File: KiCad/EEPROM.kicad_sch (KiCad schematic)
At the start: 2 parts, among them U1 24LC256

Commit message: Arreglada la EEPROM
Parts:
- renumbered U1 to U10
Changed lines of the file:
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@@
 		(on_board yes)
 		(dnp no)
-		(property "Reference" "C1"
+		(property "Reference" "C?"
 			(at 128.27 92.456 0)
 			(effects
@@
 				(path "/b59472fa-fde6-436b-a51b-1bcdb1fd69b0"
 					(reference "C1")
+					(unit 1)
+				)
+			)
+			(project "SEIENTS_EDD"
+				(path "/b6401b4f-5426-49b8-bb2e-8ecdb19989ef/e3788a6e-8f47-444e-9f2c-8c4ecda69c18"
+					(reference "C?")
 					(unit 1)
 				)
@@
 		(dnp no)
 		(fields_autoplaced yes)
-		(property "Reference" "#PWR05"
+		(property "Reference" "#PWR036"
 			(at 125.73 115.57 0)
 			(effects
@@
 		(dnp no)
 		(fields_autoplaced yes)
-		(property "Reference" "#PWR06"
+		(property "Reference" "#PWR?"
 			(at 162.56 109.22 0)
 			(effects
@@
 				(path "/b59472fa-fde6-436b-a51b-1bcdb1fd69b0"
 					(reference "#PWR06")
+					(unit 1)
+				)
+			)
+			(project "SEIENTS_EDD"
+				(path "/b6401b4f-5426-49b8-bb2e-8ecdb19989ef/e3788a6e-8f47-444e-9f2c-8c4ecda69c18"
+					(reference "#PWR?")
 					(unit 1)
 				)
@@
 		(dnp no)
 		(fields_autoplaced yes)
-		(property "Reference" "U1"
+		(property "Reference" "U10"
 			(at 150.7333 87.63 0)
 			(effects
@@
 		(dnp no)
 		(fields_autoplaced yes)
-		(property "Reference" "#PWR04"
+		(property "Reference" "#PWR035"
 			(at 148.59 115.57 0)
 			(effects
@@
 		(dnp no)
 		(fields_autoplaced yes)
-		(property "Reference" "#PWR01"
+		(property "Reference" "#PWR?"
 			(at 134.62 115.57 0)
 			(effects
@@
 					(unit 1)
 				)
+			)
+			(project "SEIENTS_EDD"
+				(path "/b6401b4f-5426-49b8-bb2e-8ecdb19989ef/e3788a6e-8f47-444e-9f2c-8c4ecda69c18"
+					(reference "#PWR?")
+					(unit 1)
+				)

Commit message: Arreglat el DE-9
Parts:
- renumbered C1 to C20
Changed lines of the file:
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@@
+	)
+	(junction
+		(at 134.62 109.22)
+		(diameter 0)
+		(color 0 0 0 0)
 	)
 	(junction
@@
 		(on_board yes)
 		(dnp no)
-		(property "Reference" "C?"
-			(at 128.27 92.456 0)
+		(property "Reference" "C20"
+			(at 128.778 94.488 0)
 			(effects
 				(font
@@
 			(project "SEIENTS_EDD"
 				(path "/b6401b4f-5426-49b8-bb2e-8ecdb19989ef/e3788a6e-8f47-444e-9f2c-8c4ecda69c18"
-					(reference "C?")
+					(reference "C20")
 					(unit 1)
 				)
@@
 		(dnp no)
 		(fields_autoplaced yes)
-		(property "Reference" "#PWR?"
+		(property "Reference" "#PWR0101"
 			(at 162.56 109.22 0)
 			(effects
@@
 			(project "SEIENTS_EDD"
 				(path "/b6401b4f-5426-49b8-bb2e-8ecdb19989ef/e3788a6e-8f47-444e-9f2c-8c4ecda69c18"
-					(reference "#PWR?")
+					(reference "#PWR0101")
 					(unit 1)
 				)
@@
 	)
 	(symbol
+		(lib_id "power:PWR_FLAG")
+		(at 134.62 109.22 270)
+		(unit 1)
+		(exclude_from_sim no)
+		(in_bom yes)
+		(on_board yes)
+		(dnp no)
+		(fields_autoplaced yes)
+		(property "Reference" "#FLG05"
+			(at 136.525 109.22 0)
+			(effects
+				(font
+					(size 1.27 1.27)
+				)
+				(hide yes)
+			)
+		)
+		(property "Value" "PWR_FLAG"
+			(at 138.43 109.2199 90)
+			(effects
+				(font
+					(size 1.27 1.27)
+				)
+				(justify left)
+			)
+		)
+		(property "Footprint" ""
+			(at 134.62 109.22 0)
+			(effects
+				(font
+					(size 1.27 1.27)
+				)
+				(hide yes)
+			)
+		)
+		(property "Datasheet" "~"
+			(at 134.62 109.22 0)
+			(effects
+				(font
+					(size 1.27 1.27)
+				)
+				(hide yes)
+			)
+		)
+		(property "Description" "Special symbol for telling ERC where power comes from"
+			(at 134.62 109.22 0)
+			(effects
+				(font
+					(size 1.27 1.27)
+				)
+				(hide yes)
+			)
+		)
+		(pin "1"
+		)
+		(instances
+			(project ""
+				(path "/b6401b4f-5426-49b8-bb2e-8ecdb19989ef/e3788a6e-8f47-444e-9f2c-8c4ecda69c18"
+					(reference "#FLG05")
+					(unit 1)
+				)
+			)
+		)
+	)
+	(symbol
 		(lib_id "power:GND")
 		(at 134.62 109.22 0)
@@
 		(dnp no)
 		(fields_autoplaced yes)
-		(property "Reference" "#PWR?"
+		(property "Reference" "#PWR0102"
 			(at 134.62 115.57 0)
 			(effects
@@
 			(project "SEIENTS_EDD"
 				(path "/b6401b4f-5426-49b8-bb2e-8ecdb19989ef/e3788a6e-8f47-444e-9f2c-8c4ecda69c18"
-					(reference "#PWR?")
-					(unit 1)
-				)
+					(reference "#PWR0102")
+					(unit 1)
+				)

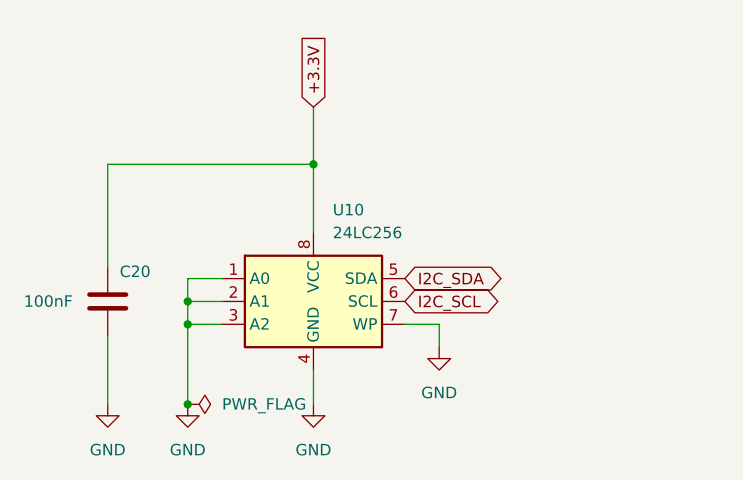
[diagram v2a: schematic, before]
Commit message: ArregLATS ERRORS ERC
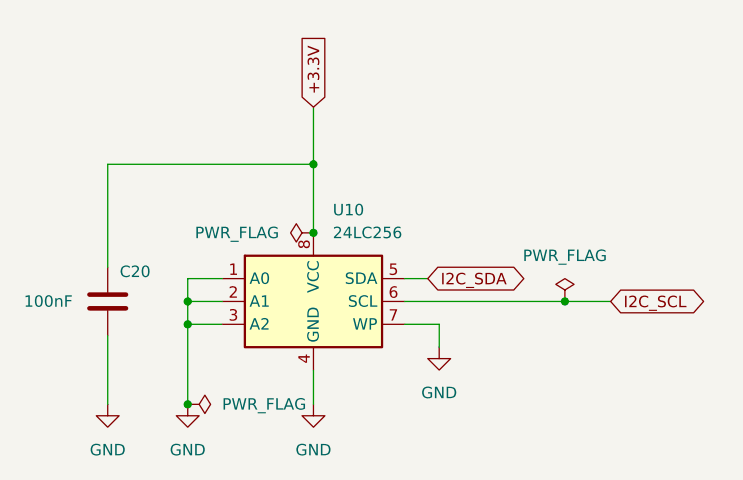
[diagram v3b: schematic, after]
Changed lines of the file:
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@@
+	)
+	(junction
+		(at 176.53 97.79)
+		(diameter 0)
+		(color 0 0 0 0)
+	)
+	(junction
+		(at 148.59 90.17)
+		(diameter 0)
+		(color 0 0 0 0)
 	)
 	(junction
@@
 	(wire
 		(pts
+			(xy 176.53 97.79) (xy 158.75 97.79)
+		)
+		(stroke
+			(width 0)
+			(type default)
+		)
+	)
+	(wire
+		(pts
 			(xy 148.59 105.41) (xy 148.59 109.22)
 		)
@@
 	(wire
 		(pts
+			(xy 161.29 95.25) (xy 158.75 95.25)
+		)
+		(stroke
+			(width 0)
+			(type default)
+		)
+	)
+	(wire
+		(pts
 			(xy 158.75 100.33) (xy 162.56 100.33)
+		)
+		(stroke
+			(width 0)
+			(type default)
+		)
+	)
+	(wire
+		(pts
+			(xy 181.61 97.79) (xy 176.53 97.79)
 		)
 		(stroke
@@
 	(global_label "I2C_SDA"
 		(shape bidirectional)
-		(at 158.75 95.25 0)
+		(at 161.29 95.25 0)
 		(fields_autoplaced yes)
 		(effects
@@
 		)
 		(property "Intersheetrefs" "${INTERSHEET_REFS}"
-			(at 170.4665 95.25 0)
+			(at 173.0065 95.25 0)
 			(effects
 				(font
@@
 	(global_label "I2C_SCL"
 		(shape bidirectional)
-		(at 158.75 97.79 0)
+		(at 181.61 97.79 0)
 		(fields_autoplaced yes)
 		(effects
@@
 		)
 		(property "Intersheetrefs" "${INTERSHEET_REFS}"
-			(at 170.406 97.79 0)
+			(at 193.266 97.79 0)
 			(effects
 				(font
@@
 				(justify left)
 				(hide yes)
+			)
+		)
+	)
+	(symbol
+		(lib_id "power:PWR_FLAG")
+		(at 176.53 97.79 0)
+		(unit 1)
+		(exclude_from_sim no)
+		(in_bom yes)
+		(on_board yes)
+		(dnp no)
+		(fields_autoplaced yes)
+		(property "Reference" "#FLG?"
+			(at 176.53 95.885 0)
+			(effects
+				(font
+					(size 1.27 1.27)
+				)
+				(hide yes)
+			)
+		)
+		(property "Value" "PWR_FLAG"
+			(at 176.53 92.71 0)
+			(effects
+				(font
+					(size 1.27 1.27)
+				)
+			)
+		)
+		(property "Footprint" ""
+			(at 176.53 97.79 0)
+			(effects
+				(font
+					(size 1.27 1.27)
+				)
+				(hide yes)
+			)
+		)
+		(property "Datasheet" "~"
+			(at 176.53 97.79 0)
+			(effects
+				(font
+					(size 1.27 1.27)
+				)
+				(hide yes)
+			)
+		)
+		(property "Description" "Special symbol for telling ERC where power comes from"
+			(at 176.53 97.79 0)
+			(effects
+				(font
+					(size 1.27 1.27)
+				)
+				(hide yes)
+			)
+		)
+		(pin "1"
+		)
+		(instances
+			(project "EEPROM"
+				(path "/b59472fa-fde6-436b-a51b-1bcdb1fd69b0"
+					(reference "#FLG02")
+					(unit 1)
+				)
+			)
+			(project "SEIENTS_EDD"
+				(path "/b6401b4f-5426-49b8-bb2e-8ecdb19989ef/e3788a6e-8f47-444e-9f2c-8c4ecda69c18"
+					(reference "#FLG?")
+					(unit 1)
+				)
 			)
 		)
@@
 		)
 		(instances
+			(project "EEPROM"
+				(path "/b59472fa-fde6-436b-a51b-1bcdb1fd69b0"
+					(reference "#FLG0101")
+					(unit 1)
+				)
+			)
 			(project ""
 				(path "/b6401b4f-5426-49b8-bb2e-8ecdb19989ef/e3788a6e-8f47-444e-9f2c-8c4ecda69c18"
@@
 					(unit 1)
 				)
+			)
+		)
+	)
+	(symbol
+		(lib_id "power:PWR_FLAG")
+		(at 148.59 90.17 90)
+		(unit 1)
+		(exclude_from_sim no)
+		(in_bom yes)
+		(on_board yes)
+		(dnp no)
+		(fields_autoplaced yes)
+		(property "Reference" "#FLG?"
+			(at 146.685 90.17 0)
+			(effects
+				(font
+					(size 1.27 1.27)
+				)
+				(hide yes)
+			)
+		)
+		(property "Value" "PWR_FLAG"
+			(at 144.78 90.1699 90)
+			(effects
+				(font
+					(size 1.27 1.27)
+				)
+				(justify left)
+			)
+		)
+		(property "Footprint" ""
+			(at 148.59 90.17 0)
+			(effects
+				(font
+					(size 1.27 1.27)
+				)
+				(hide yes)
+			)
+		)
+		(property "Datasheet" "~"
+			(at 148.59 90.17 0)
+			(effects
+				(font
+					(size 1.27 1.27)
+				)
+				(hide yes)
+			)
+		)
+		(property "Description" "Special symbol for telling ERC where power comes from"
+			(at 148.59 90.17 0)
+			(effects
+				(font
+					(size 1.27 1.27)
+				)
+				(hide yes)
+			)
+		)
+		(pin "1"
+		)
+		(instances
+			(project ""
+				(path "/b59472fa-fde6-436b-a51b-1bcdb1fd69b0"
+					(reference "#FLG01")
+					(unit 1)
+				)
+			)
+			(project "SEIENTS_EDD"
+				(path "/b6401b4f-5426-49b8-bb2e-8ecdb19989ef/e3788a6e-8f47-444e-9f2c-8c4ecda69c18"
+					(reference "#FLG?")
+					(unit 1)
+				)

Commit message: canvia al microcontrolador
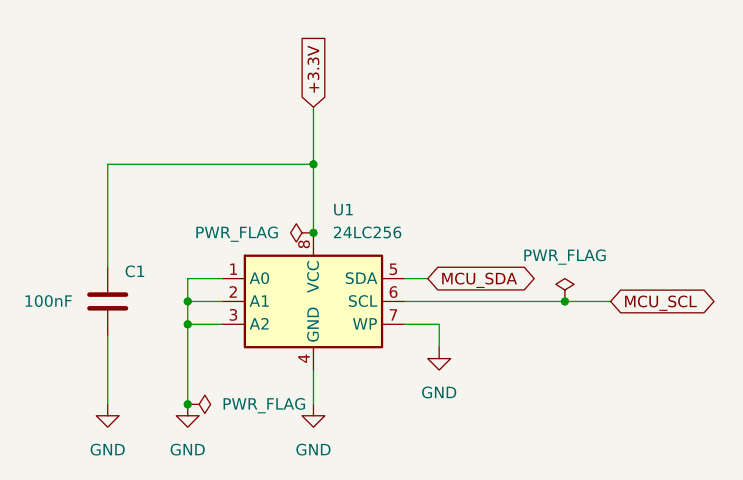
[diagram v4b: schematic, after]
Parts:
- renumbered C20 to C1, U10 to U1
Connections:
- net I2C_SCL renamed MCU_SCL
- net I2C_SDA renamed MCU_SDA
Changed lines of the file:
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@@
 		)
 	)
-	(global_label "I2C_SDA"
+	(global_label "MCU_SDA"
 		(shape bidirectional)
 		(at 161.29 95.25 0)
@@
 		)
 		(property "Intersheetrefs" "${INTERSHEET_REFS}"
-			(at 173.0065 95.25 0)
+			(at 173.9741 95.25 0)
 			(effects
 				(font
@@
 		)
 	)
-	(global_label "I2C_SCL"
+	(global_label "MCU_SCL"
 		(shape bidirectional)
 		(at 181.61 97.79 0)
@@
 		)
 		(property "Intersheetrefs" "${INTERSHEET_REFS}"
-			(at 193.266 97.79 0)
+			(at 194.2336 97.79 0)
 			(effects
 				(font
@@
 		(dnp no)
 		(fields_autoplaced yes)
-		(property "Reference" "#FLG?"
+		(property "Reference" "#FLG02"
 			(at 176.53 95.885 0)
 			(effects
@@
 		(on_board yes)
 		(dnp no)
-		(property "Reference" "C20"
+		(property "Reference" "C1"
 			(at 128.778 94.488 0)
 			(effects
@@
 		(dnp no)
 		(fields_autoplaced yes)
-		(property "Reference" "#PWR036"
+		(property "Reference" "#PWR05"
 			(at 125.73 115.57 0)
 			(effects
@@
 		(dnp no)
 		(fields_autoplaced yes)
-		(property "Reference" "#PWR0101"
+		(property "Reference" "#PWR06"
 			(at 162.56 109.22 0)
 			(effects
@@
 		(dnp no)
 		(fields_autoplaced yes)
-		(property "Reference" "U10"
+		(property "Reference" "U1"
 			(at 150.7333 87.63 0)
 			(effects
@@
 		(dnp no)
 		(fields_autoplaced yes)
-		(property "Reference" "#PWR035"
+		(property "Reference" "#PWR04"
 			(at 148.59 115.57 0)
 			(effects
@@
 		(dnp no)
 		(fields_autoplaced yes)
-		(property "Reference" "#FLG05"
+		(property "Reference" "#FLG0101"
 			(at 136.525 109.22 0)
 			(effects
@@
 		(dnp no)
 		(fields_autoplaced yes)
-		(property "Reference" "#PWR0102"
+		(property "Reference" "#PWR01"
 			(at 134.62 115.57 0)
 			(effects
@@
 		(dnp no)
 		(fields_autoplaced yes)
-		(property "Reference" "#FLG?"
+		(property "Reference" "#FLG01"
 			(at 146.685 90.17 0)
 			(effects

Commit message: Modificacions Micro
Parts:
- renumbered C1 to C20, U1 to U10
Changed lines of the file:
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@@
-	)
-	(junction
-		(at 148.59 90.17)
-		(diameter 0)
-		(color 0 0 0 0)
-	)
-	(junction
-		(at 134.62 109.22)
-		(diameter 0)
-		(color 0 0 0 0)
 	)
 	(junction
@@
 		(dnp no)
 		(fields_autoplaced yes)
-		(property "Reference" "#FLG02"
+		(property "Reference" "#FLG017"
 			(at 176.53 95.885 0)
 			(effects
@@
 			(project "SEIENTS_EDD"
 				(path "/b6401b4f-5426-49b8-bb2e-8ecdb19989ef/e3788a6e-8f47-444e-9f2c-8c4ecda69c18"
-					(reference "#FLG?")
+					(reference "#FLG017")
 					(unit 1)
 				)
@@
 		(on_board yes)
 		(dnp no)
-		(property "Reference" "C1"
+		(property "Reference" "C20"
 			(at 128.778 94.488 0)
 			(effects
@@
 		(dnp no)
 		(fields_autoplaced yes)
-		(property "Reference" "#PWR05"
+		(property "Reference" "#PWR036"
 			(at 125.73 115.57 0)
 			(effects
@@
 		(dnp no)
 		(fields_autoplaced yes)
-		(property "Reference" "#PWR06"
+		(property "Reference" "#PWR0101"
 			(at 162.56 109.22 0)
 			(effects
@@
 		(dnp no)
 		(fields_autoplaced yes)
-		(property "Reference" "U1"
+		(property "Reference" "U10"
 			(at 150.7333 87.63 0)
 			(effects
@@
 		(dnp no)
 		(fields_autoplaced yes)
-		(property "Reference" "#PWR04"
+		(property "Reference" "#PWR035"
 			(at 148.59 115.57 0)
 			(effects
@@
 				(path "/b6401b4f-5426-49b8-bb2e-8ecdb19989ef/e3788a6e-8f47-444e-9f2c-8c4ecda69c18"
 					(reference "#PWR035")
-					(unit 1)
-				)
-			)
-		)
-	)
-	(symbol
-		(lib_id "power:PWR_FLAG")
-		(at 134.62 109.22 270)
-		(unit 1)
-		(exclude_from_sim no)
-		(in_bom yes)
-		(on_board yes)
-		(dnp no)
-		(fields_autoplaced yes)
-		(property "Reference" "#FLG0101"
-			(at 136.525 109.22 0)
-			(effects
-				(font
-					(size 1.27 1.27)
-				)
-				(hide yes)
-			)
-		)
-		(property "Value" "PWR_FLAG"
-			(at 138.43 109.2199 90)
-			(effects
-				(font
-					(size 1.27 1.27)
-				)
-				(justify left)
-			)
-		)
-		(property "Footprint" ""
-			(at 134.62 109.22 0)
-			(effects
-				(font
-					(size 1.27 1.27)
-				)
-				(hide yes)
-			)
-		)
-		(property "Datasheet" "~"
-			(at 134.62 109.22 0)
-			(effects
-				(font
-					(size 1.27 1.27)
-				)
-				(hide yes)
-			)
-		)
-		(property "Description" "Special symbol for telling ERC where power comes from"
-			(at 134.62 109.22 0)
-			(effects
-				(font
-					(size 1.27 1.27)
-				)
-				(hide yes)
-			)
-		)
-		(pin "1"
-		)
-		(instances
-			(project "EEPROM"
-				(path "/b59472fa-fde6-436b-a51b-1bcdb1fd69b0"
-					(reference "#FLG0101")
-					(unit 1)
-				)
-			)
-			(project ""
-				(path "/b6401b4f-5426-49b8-bb2e-8ecdb19989ef/e3788a6e-8f47-444e-9f2c-8c4ecda69c18"
-					(reference "#FLG05")
 					(unit 1)
 				)
@@
 		(dnp no)
 		(fields_autoplaced yes)
-		(property "Reference" "#PWR01"
+		(property "Reference" "#PWR0102"
 			(at 134.62 115.57 0)
 			(effects
@@
 					(unit 1)
 				)
-			)
-		)
-	)
-	(symbol
-		(lib_id "power:PWR_FLAG")
-		(at 148.59 90.17 90)
-		(unit 1)
-		(exclude_from_sim no)
-		(in_bom yes)
-		(on_board yes)
-		(dnp no)
-		(fields_autoplaced yes)
-		(property "Reference" "#FLG01"
-			(at 146.685 90.17 0)
-			(effects
-				(font
-					(size 1.27 1.27)
-				)
-				(hide yes)
-			)
-		)
-		(property "Value" "PWR_FLAG"
-			(at 144.78 90.1699 90)
-			(effects
-				(font
-					(size 1.27 1.27)
-				)
-				(justify left)
-			)
-		)
-		(property "Footprint" ""
-			(at 148.59 90.17 0)
-			(effects
-				(font
-					(size 1.27 1.27)
-				)
-				(hide yes)
-			)
-		)
-		(property "Datasheet" "~"
-			(at 148.59 90.17 0)
-			(effects
-				(font
-					(size 1.27 1.27)
-				)
-				(hide yes)
-			)
-		)
-		(property "Description" "Special symbol for telling ERC where power comes from"
-			(at 148.59 90.17 0)
-			(effects
-				(font
-					(size 1.27 1.27)
-				)
-				(hide yes)
-			)
-		)
-		(pin "1"
-		)
-		(instances
-			(project ""
-				(path "/b59472fa-fde6-436b-a51b-1bcdb1fd69b0"
-					(reference "#FLG01")
-					(unit 1)
-				)
-			)
-			(project "SEIENTS_EDD"
-				(path "/b6401b4f-5426-49b8-bb2e-8ecdb19989ef/e3788a6e-8f47-444e-9f2c-8c4ecda69c18"
-					(reference "#FLG?")
-					(unit 1)
-				)

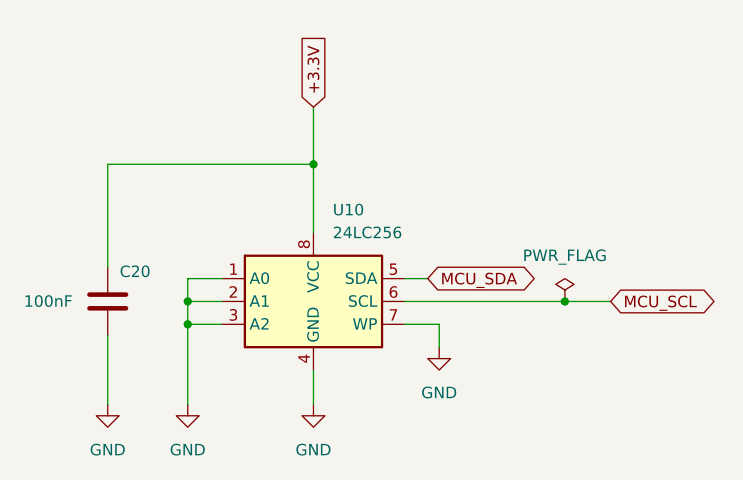
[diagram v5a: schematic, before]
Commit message: Començat el LAYOUT
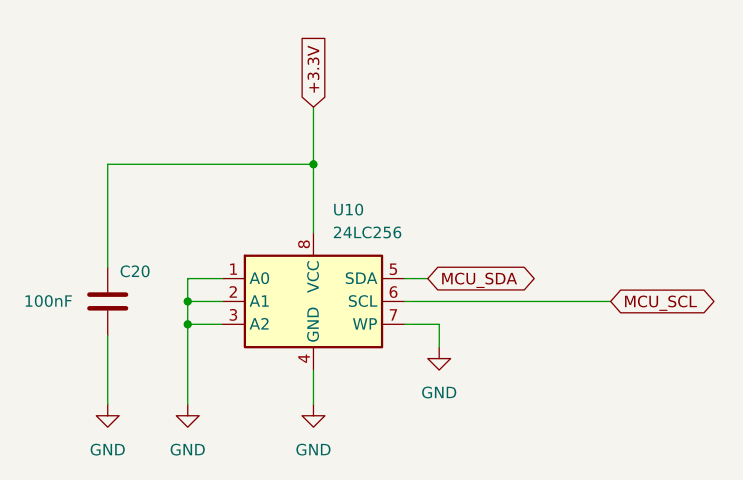
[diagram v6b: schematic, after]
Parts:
- U10: footprint (none) -> Package_SO:SOIC-16_3.9x9.9mm_P1.27mm
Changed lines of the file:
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@@
-	)
-	(junction
-		(at 176.53 97.79)
-		(diameter 0)
-		(color 0 0 0 0)
 	)
 	(junction
@@
 	(wire
 		(pts
-			(xy 176.53 97.79) (xy 158.75 97.79)
+			(xy 158.75 97.79) (xy 181.61 97.79)
 		)
 		(stroke
@@
 		(pts
 			(xy 158.75 100.33) (xy 162.56 100.33)
-		)
-		(stroke
-			(width 0)
-			(type default)
-		)
-	)
-	(wire
-		(pts
-			(xy 181.61 97.79) (xy 176.53 97.79)
 		)
 		(stroke
@@
 				(justify left)
 				(hide yes)
-			)
-		)
-	)
-	(symbol
-		(lib_id "power:PWR_FLAG")
-		(at 176.53 97.79 0)
-		(unit 1)
-		(exclude_from_sim no)
-		(in_bom yes)
-		(on_board yes)
-		(dnp no)
-		(fields_autoplaced yes)
-		(property "Reference" "#FLG017"
-			(at 176.53 95.885 0)
-			(effects
-				(font
-					(size 1.27 1.27)
-				)
-				(hide yes)
-			)
-		)
-		(property "Value" "PWR_FLAG"
-			(at 176.53 92.71 0)
-			(effects
-				(font
-					(size 1.27 1.27)
-				)
-			)
-		)
-		(property "Footprint" ""
-			(at 176.53 97.79 0)
-			(effects
-				(font
-					(size 1.27 1.27)
-				)
-				(hide yes)
-			)
-		)
-		(property "Datasheet" "~"
-			(at 176.53 97.79 0)
-			(effects
-				(font
-					(size 1.27 1.27)
-				)
-				(hide yes)
-			)
-		)
-		(property "Description" "Special symbol for telling ERC where power comes from"
-			(at 176.53 97.79 0)
-			(effects
-				(font
-					(size 1.27 1.27)
-				)
-				(hide yes)
-			)
-		)
-		(pin "1"
-		)
-		(instances
-			(project "EEPROM"
-				(path "/b59472fa-fde6-436b-a51b-1bcdb1fd69b0"
-					(reference "#FLG02")
-					(unit 1)
-				)
-			)
-			(project "SEIENTS_EDD"
-				(path "/b6401b4f-5426-49b8-bb2e-8ecdb19989ef/e3788a6e-8f47-444e-9f2c-8c4ecda69c18"
-					(reference "#FLG017")
-					(unit 1)
-				)
 			)
 		)
@@
 			)
 		)
-		(property "Footprint" ""
+		(property "Footprint" "Package_SO:SOIC-16_3.9x9.9mm_P1.27mm"
 			(at 148.59 97.79 0)
 			(effects

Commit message: footprints asignados
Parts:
- C20: footprint (none) -> Capacitor_SMD:C_0805_2012Metric
- U10: footprint Package_SO:SOIC-16_3.9x9.9mm_P1.27mm -> Package_SO:SOIC-8_3.9x4.9mm_P1.27mm
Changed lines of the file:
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@@
 			)
 		)
-		(property "Footprint" ""
+		(property "Footprint" "Capacitor_SMD:C_0805_2012Metric"
 			(at 124.7648 93.98 0)
 			(effects
@@
 			)
 		)
-		(property "Footprint" "Package_SO:SOIC-16_3.9x9.9mm_P1.27mm"
+		(property "Footprint" "Package_SO:SOIC-8_3.9x4.9mm_P1.27mm"
 			(at 148.59 97.79 0)
 			(effects
